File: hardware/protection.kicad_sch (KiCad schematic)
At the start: 12 parts

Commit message: Alpha 1.0.0 Schematic
First Schematic Version for initial checkup
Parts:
- removed R?: R, symbol Device:R
- C? (x4): value C -> 100nF
- R? (x2): value R -> 1k
- R?: value R -> 1K
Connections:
- net SAFETY_IN_P is gone; now on net SAFETY_IN: C?.1
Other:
- note added: "24v"
- note added: "3V3"
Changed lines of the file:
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@@
     (stroke (width 0) (type default) (color 0 0 0 0))
   )
-  (wire (pts (xy 72.39 77.47) (xy 78.74 77.47))
+  (wire (pts (xy 72.39 77.47) (xy 91.44 77.47))
     (stroke (width 0) (type default) (color 0 0 0 0))
   )
@@
   )
   (wire (pts (xy 72.39 91.44) (xy 72.39 87.63))
-    (stroke (width 0) (type default) (color 0 0 0 0))
-  )
-  (wire (pts (xy 86.36 77.47) (xy 91.44 77.47))
     (stroke (width 0) (type default) (color 0 0 0 0))
   )
@@
     (effects (font (size 1.27 1.27) italic) (justify left bottom))
   )
+  (text "3V3" (at 63.5 115.57 0)
+    (effects (font (size 1.27 1.27) italic) (justify left bottom))
+  )
+  (text "3V3" (at 62.23 144.78 0)
+    (effects (font (size 1.27 1.27) italic) (justify left bottom))
+  )
+  (text "24v\n" (at 64.77 86.36 0)
+    (effects (font (size 1.27 1.27) italic) (justify left bottom))
+  )
+  (text "24v\n" (at 66.04 48.26 0)
+    (effects (font (size 1.27 1.27) italic) (justify left bottom))
+  )
   (hierarchical_label "SAFETY_IN_P" (shape output) (at 107.95 77.47 0)
     (effects (font (size 1.27 1.27)) (justify left))
@@
     (effects (font (size 1.27 1.27)) (justify left))
   )
-  (symbol (lib_id "Device:R") (at 82.55 77.47 270) (unit 1)
-    (in_bom yes) (on_board yes) (fields_autoplaced)
-    (property "Reference" "R?" (id 0) (at 82.55 71.12 90))
-    (property "Value" "R" (id 1) (at 82.55 73.66 90))
-    (property "Footprint" "" (id 2) (at 82.55 75.692 90)
-      (effects (font (size 1.27 1.27)) hide)
-    )
-    (property "Datasheet" "~" (id 3) (at 82.55 77.47 0)
-      (effects (font (size 1.27 1.27)) hide)
-    )
-    (pin "1")
-    (pin "2")
-  )
   (symbol (lib_id "Device:C") (at 91.44 46.99 0) (unit 1)
     (in_bom yes) (on_board yes) (fields_autoplaced)
@@
       (effects (font (size 1.27 1.27)) (justify left))
     )
-    (property "Value" "C" (id 1) (at 95.25 48.2599 0)
+    (property "Value" "100nF" (id 1) (at 95.25 48.2599 0)
       (effects (font (size 1.27 1.27)) (justify left))
     )
@@
       (effects (font (size 1.27 1.27)) (justify left))
     )
-    (property "Value" "C" (id 1) (at 95.25 85.0899 0)
+    (property "Value" "100nF" (id 1) (at 95.25 85.0899 0)
       (effects (font (size 1.27 1.27)) (justify left))
     )
@@
       (effects (font (size 1.27 1.27)) (justify left))
     )
-    (property "Value" "C" (id 1) (at 96.52 147.3199 0)
+    (property "Value" "100nF" (id 1) (at 96.52 147.3199 0)
       (effects (font (size 1.27 1.27)) (justify left))
     )
@@
     (in_bom yes) (on_board yes)
     (property "Reference" "R?" (id 0) (at 82.55 102.87 90))
-    (property "Value" "R" (id 1) (at 82.55 105.41 90))
+    (property "Value" "1k" (id 1) (at 82.55 105.41 90))
     (property "Footprint" "" (id 2) (at 82.55 107.442 90)
       (effects (font (size 1.27 1.27)) hide)
@@
     (in_bom yes) (on_board yes)
     (property "Reference" "R?" (id 0) (at 83.82 146.05 90))
-    (property "Value" "R" (id 1) (at 83.82 143.51 90))
+    (property "Value" "1k" (id 1) (at 83.82 143.51 90))
     (property "Footprint" "" (id 2) (at 83.82 141.478 90)
       (effects (font (size 1.27 1.27)) hide)
@@
     (in_bom yes) (on_board yes) (fields_autoplaced)
     (property "Reference" "R?" (id 0) (at 82.55 34.29 90))
-    (property "Value" "R" (id 1) (at 82.55 36.83 90))
+    (property "Value" "1K" (id 1) (at 82.55 36.83 90))
     (property "Footprint" "" (id 2) (at 82.55 38.862 90)
       (effects (font (size 1.27 1.27)) hide)
@@
       (effects (font (size 1.27 1.27)) (justify left))
     )
-    (property "Value" "C" (id 1) (at 95.25 116.8399 0)
-      (effects (font (size 1.27 1.27)) (justify left))
-    )
+    (property "Value" "100nF" (id 1) (at 95.25 116.8399 0)
+      (effects (font (size 1.27 1.27)) (justify left))
+    )

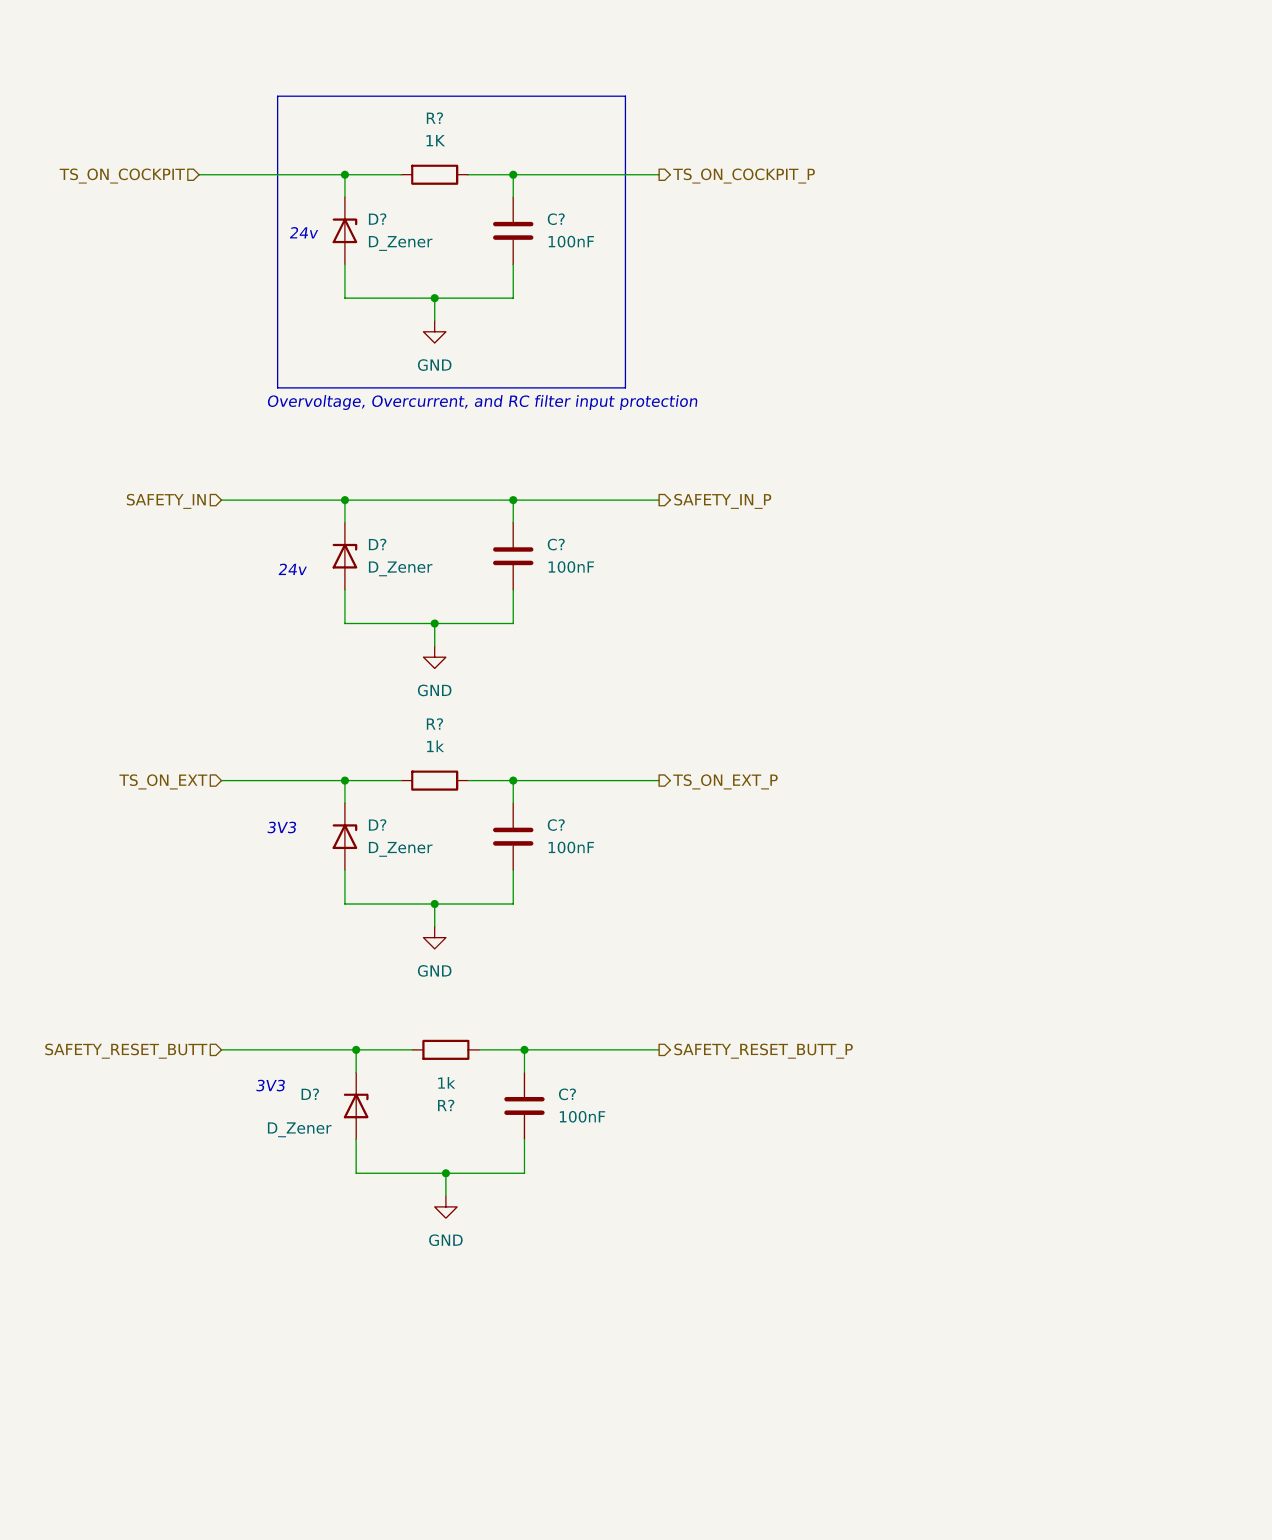
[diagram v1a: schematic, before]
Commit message: Minor changes on v1 schematic
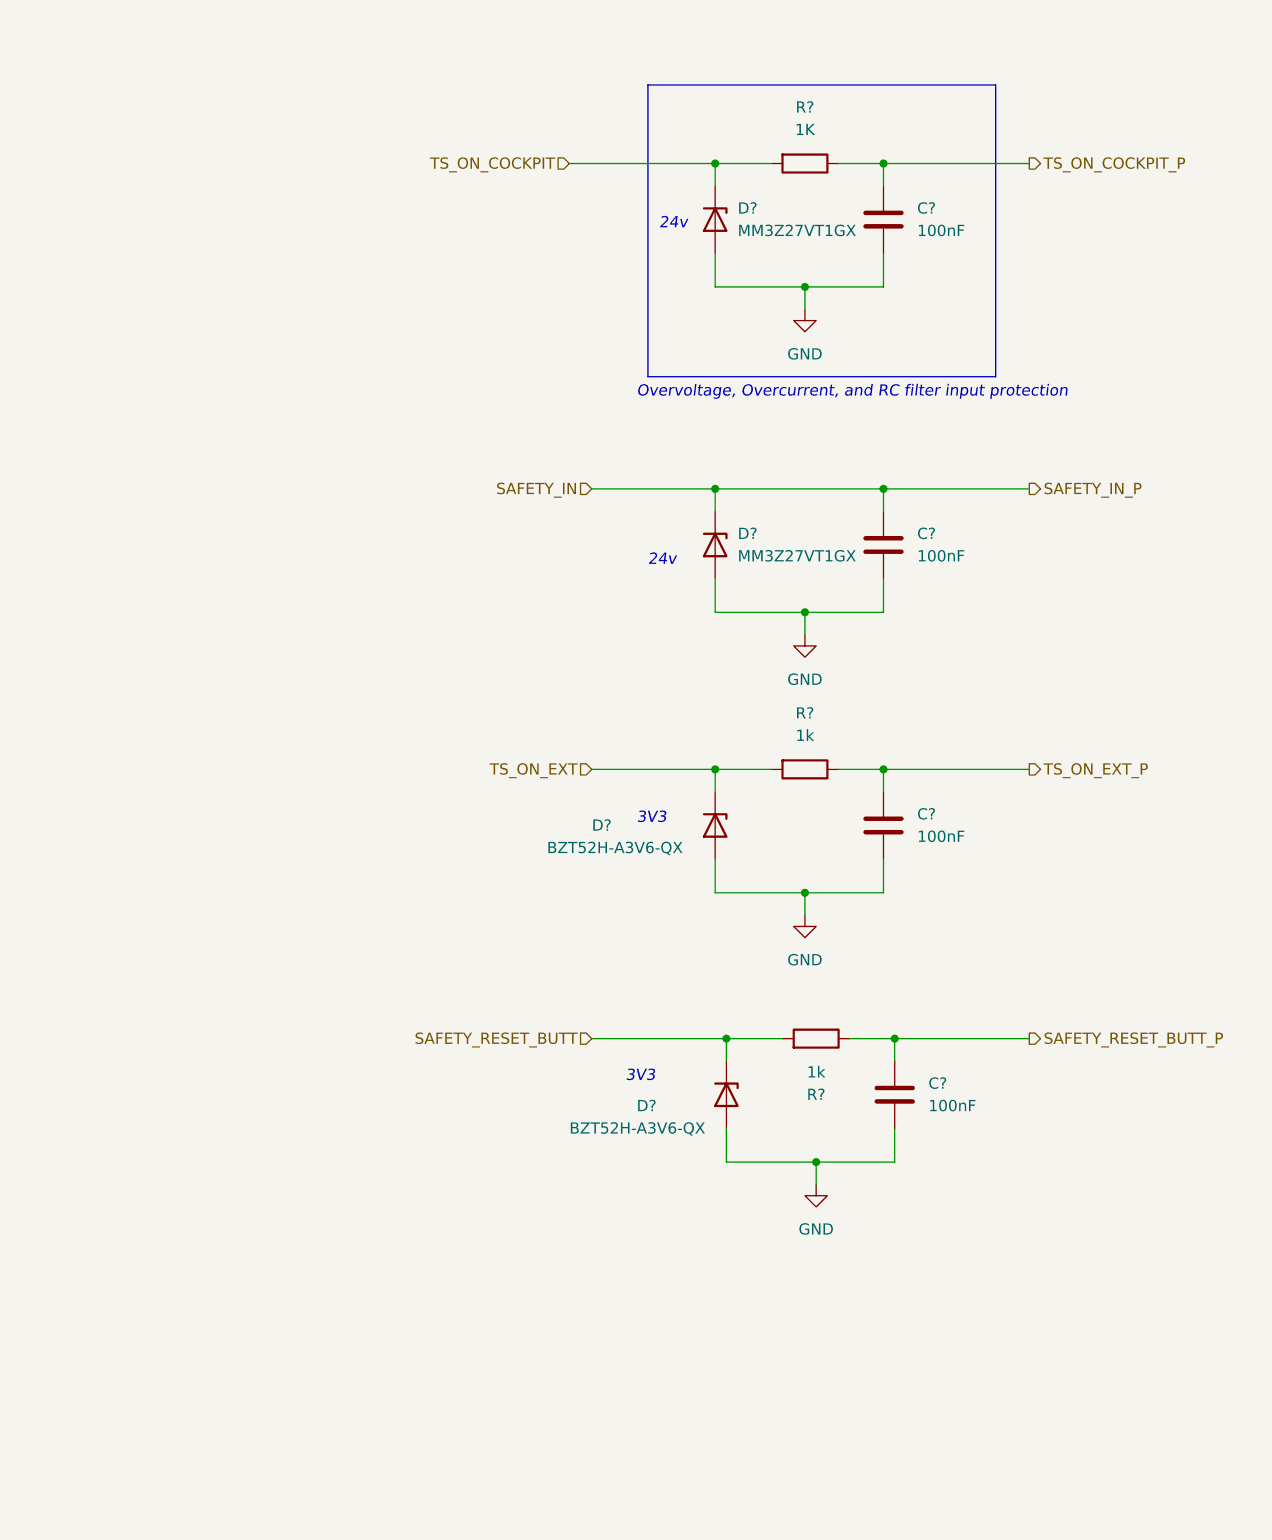
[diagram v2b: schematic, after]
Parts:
- D? (x2): value D_Zener -> MM3Z27VT1GX
- D? (x2): value D_Zener -> BZT52H-A3V6-QX
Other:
- moved on the sheet: C?, D?, R?

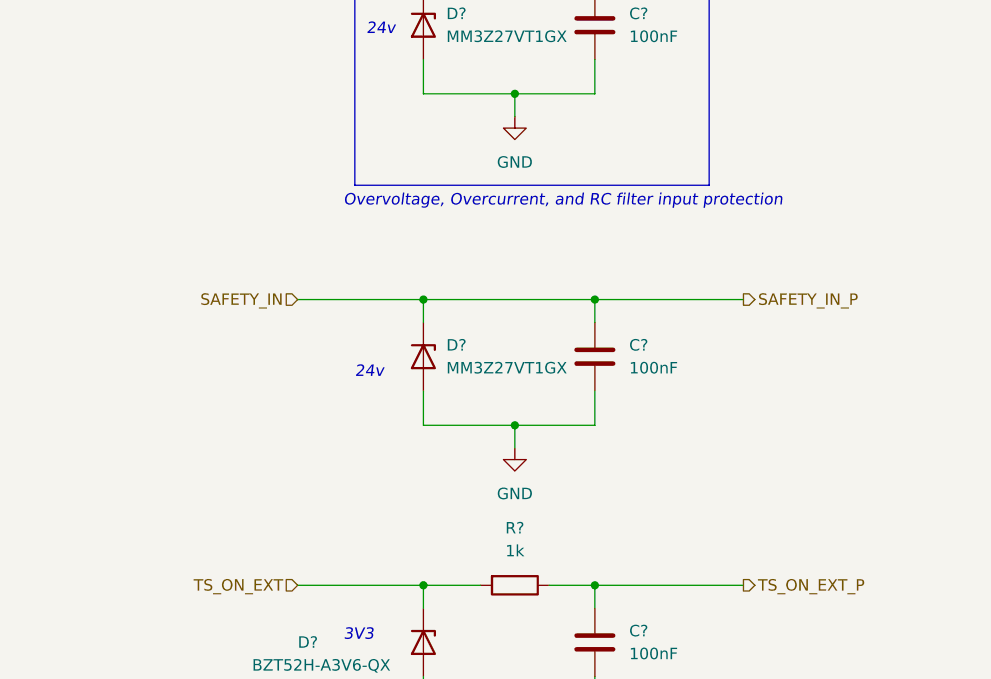
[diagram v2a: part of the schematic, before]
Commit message: minor schematic cleanup
Fixes before second review
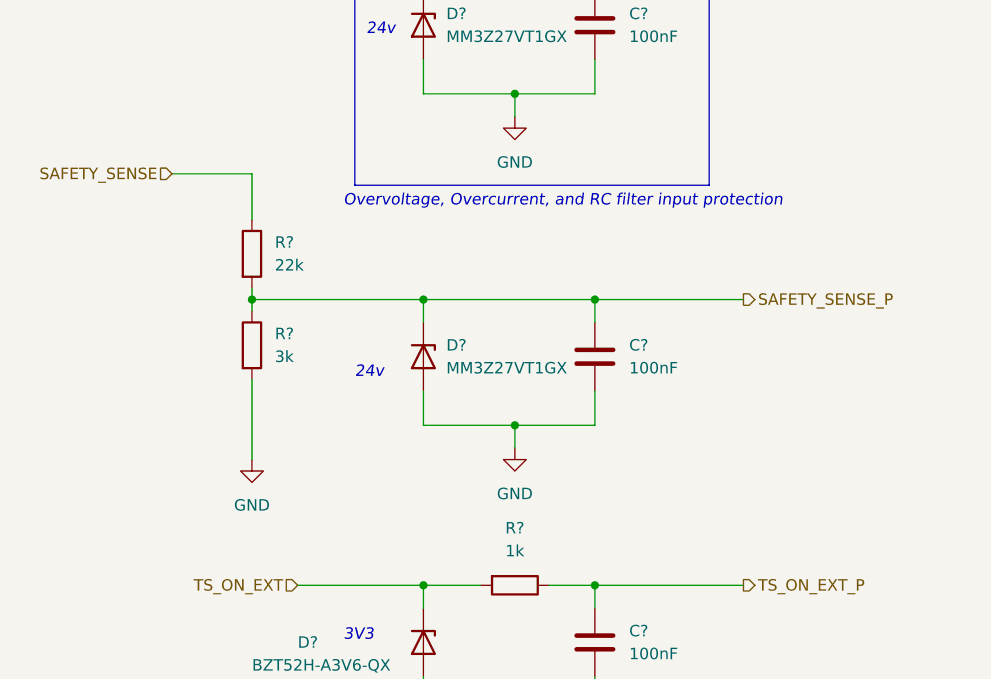
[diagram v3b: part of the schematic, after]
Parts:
- added R?: 22k, symbol Device:R
- added R?: 3k, symbol Device:R
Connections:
- net GND: now also R?.2
- net SAFETY_IN renamed SAFETY_SENSE_P
- net SAFETY_SENSE_P: now also R?.1, R?.2
- new net SAFETY_SENSE: R?.1
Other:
- company: (none) -> PUT Motorsport
- title: (none) -> Input Signals Protection
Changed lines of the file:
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@@
 (kicad_sch (version 20211123) (generator eeschema)
   (paper "A4")
+  (title_block
+    (title "Input Signals Protection")
+    (date "2022-10-29")
+    (rev "Beta 1.1")
+    (company "PUT Motorsport")
+  )
   (junction (at 134.62 138.43) (diameter 0) (color 0 0 0 0)
   )
@@
   (junction (at 114.3 76.2) (diameter 0) (color 0 0 0 0)
   )
+  (junction (at 95.25 76.2) (diameter 0) (color 0 0 0 0)
+  )
   (junction (at 115.57 138.43) (diameter 0) (color 0 0 0 0)
   )
@@
     (stroke (width 0) (type default) (color 0 0 0 0))
   )
+  (wire (pts (xy 95.25 62.23) (xy 86.36 62.23))
+    (stroke (width 0) (type default) (color 0 0 0 0))
+  )
   (wire (pts (xy 133.35 39.37) (xy 149.86 39.37))
     (stroke (width 0) (type default) (color 0 0 0 0))
@@
     (stroke (width 0) (type default) (color 0 0 0 0))
   )
+  (wire (pts (xy 95.25 76.2) (xy 95.25 77.47))
+    (stroke (width 0) (type default) (color 0 0 0 0))
+  )
   (wire (pts (xy 124.46 90.17) (xy 133.35 90.17))
     (stroke (width 0) (type default) (color 0 0 0 0))
@@
     (stroke (width 0) (type default) (color 0 0 0 0))
   )
+  (wire (pts (xy 95.25 85.09) (xy 95.25 93.98))
+    (stroke (width 0) (type default) (color 0 0 0 0))
+  )
   (wire (pts (xy 134.62 148.59) (xy 134.62 152.4))
     (stroke (width 0) (type default) (color 0 0 0 0))
@@
     (stroke (width 0) (type default) (color 0 0 0 0))
   )
+  (wire (pts (xy 95.25 67.31) (xy 95.25 62.23))
+    (stroke (width 0) (type default) (color 0 0 0 0))
+  )
   (wire (pts (xy 114.3 53.34) (xy 114.3 49.53))
     (stroke (width 0) (type default) (color 0 0 0 0))
@@
     (stroke (width 0) (type default) (color 0 0 0 0))
   )
+  (wire (pts (xy 95.25 74.93) (xy 95.25 76.2))
+    (stroke (width 0) (type default) (color 0 0 0 0))
+  )
   (wire (pts (xy 115.57 152.4) (xy 115.57 148.59))
     (stroke (width 0) (type default) (color 0 0 0 0))
@@
     (stroke (width 0) (type default) (color 0 0 0 0))
   )
-  (wire (pts (xy 100.33 76.2) (xy 114.3 76.2))
+  (wire (pts (xy 95.25 76.2) (xy 114.3 76.2))
     (stroke (width 0) (type default) (color 0 0 0 0))
   )
@@
     (effects (font (size 1.27 1.27) italic) (justify left bottom))
   )
-  (hierarchical_label "SAFETY_IN_P" (shape output) (at 149.86 76.2 0)
+  (hierarchical_label "SAFETY_SENSE_P" (shape output) (at 149.86 76.2 0)
     (effects (font (size 1.27 1.27)) (justify left))
+  )
+  (hierarchical_label "SAFETY_SENSE" (shape input) (at 86.36 62.23 180)
+    (effects (font (size 1.27 1.27)) (justify right))
   )
   (hierarchical_label "TS_ON_COCKPIT_P" (shape output) (at 149.86 39.37 0)
@@
     (effects (font (size 1.27 1.27)) (justify right))
   )
-  (hierarchical_label "SAFETY_IN" (shape input) (at 100.33 76.2 180)
-    (effects (font (size 1.27 1.27)) (justify right))
-  )
   (hierarchical_label "TS_ON_COCKPIT" (shape input) (at 97.79 39.37 180)
     (effects (font (size 1.27 1.27)) (justify right))
@@
     (pin "1")
     (pin "2")
+  )
+  (symbol (lib_id "power:GND") (at 95.25 93.98 0) (unit 1)
+    (in_bom yes) (on_board yes) (fields_autoplaced)
+    (property "Reference" "#PWR?" (id 0) (at 95.25 100.33 0)
+      (effects (font (size 1.27 1.27)) hide)
+    )
+    (property "Value" "GND" (id 1) (at 95.25 99.06 0))
+    (property "Footprint" "" (id 2) (at 95.25 93.98 0)
+      (effects (font (size 1.27 1.27)) hide)
+    )
+    (property "Datasheet" "" (id 3) (at 95.25 93.98 0)
+      (effects (font (size 1.27 1.27)) hide)
+    )
+    (pin "1")
   )
   (symbol (lib_id "power:GND") (at 124.46 55.88 0) (unit 1)
@@
       (effects (font (size 1.27 1.27)) hide)
     )
+    (pin "1")
+    (pin "2")
+  )
+  (symbol (lib_id "Device:R") (at 95.25 71.12 0) (unit 1)
+    (in_bom yes) (on_board yes) (fields_autoplaced)
+    (property "Reference" "R?" (id 0) (at 97.79 69.8499 0)
+      (effects (font (size 1.27 1.27)) (justify left))
+    )
+    (property "Value" "22k" (id 1) (at 97.79 72.3899 0)
+      (effects (font (size 1.27 1.27)) (justify left))
+    )
+    (property "Footprint" "" (id 2) (at 93.472 71.12 90)
+      (effects (font (size 1.27 1.27)) hide)
+    )
+    (property "Datasheet" "~" (id 3) (at 95.25 71.12 0)
+      (effects (font (size 1.27 1.27)) hide)
+    )
+    (pin "1")
+    (pin "2")
+  )
+  (symbol (lib_id "Device:R") (at 95.25 81.28 0) (unit 1)
+    (in_bom yes) (on_board yes) (fields_autoplaced)
+    (property "Reference" "R?" (id 0) (at 97.79 80.0099 0)
+      (effects (font (size 1.27 1.27)) (justify left))
+    )
+    (property "Value" "3k" (id 1) (at 97.79 82.5499 0)
+      (effects (font (size 1.27 1.27)) (justify left))
+    )
+    (property "Footprint" "" (id 2) (at 93.472 81.28 90)
+      (effects (font (size 1.27 1.27)) hide)
+    )
+    (property "Datasheet" "~" (id 3) (at 95.25 81.28 0)
+      (effects (font (size 1.27 1.27)) hide)
+    )
